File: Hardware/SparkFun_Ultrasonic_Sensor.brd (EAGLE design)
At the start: 44.5 x 21.5 mm, 76 parts, among them J4 Vertical Qwiic Connector, J6 Vertical Qwiic Connector, Q1 600mA/40V, U5 ULTRASONIC_SENSOR_TRANSMITTER, U6 LMV324, U7 STM8L051F3, U8 SP3232EB, U9 ULTRASONIC_SENSOR_RECEIVER

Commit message: Moves the odering instructions away from the design
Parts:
- moved LOGO1 7.62 mm to (57.1, 50.8)
- moved FRAME1 5.24 mm to (77.9, -8.87)
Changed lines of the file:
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@@
 <drawing>
 <settings>
-<setting alwaysvectorfont="no"/>
+<setting alwaysvectorfont="yes"/>
 <setting keepoldvectorfont="yes"/>
 <setting verticaltext="up"/>
@@
 <wire x1="0" y1="21.5392" x2="0" y2="0" width="0.2032" layer="20"/>
 <dimension x1="0" y1="0" x2="0" y2="21.5392" x3="-7.62" y3="10.7696" textsize="1.778" textratio="15" layer="47" unit="inch"/>
-<text x="50.8" y="22.86" size="1.778" layer="51" font="vector">Two Layer
+<text x="58.42" y="22.86" size="1.778" layer="51" font="vector">Two Layer
 1.6mm Thickness
 1 oz. Copper
@@
 HASL Lead Free
 Material: TG135-140</text>
-<text x="102.87" y="-7.62" size="1.778" layer="51" font="vector">NOA Labs</text>
-<text x="84.328" y="-10.16" size="1.778" layer="51" font="vector">Revised By: Elias Santistevan</text>
+<text x="107.95" y="-8.89" size="1.778" layer="51" font="vector">NOA Labs</text>
+<text x="89.408" y="-11.43" size="1.778" layer="51" font="vector">Revised By: Elias Santistevan</text>
 <dimension x1="0" y1="21.5392" x2="44.45" y2="21.5392" x3="22.225" y3="31.75" textsize="1.778" layer="47" unit="inch"/>
 <dimension x1="10.16" y1="12.7" x2="0" y2="12.7" x3="5.08" y3="24.13" textsize="1.778" layer="47" unit="inch"/>
@@
 <attribute name="VALUE" x="38.0746" y="9.8298" size="0.6096" layer="27" font="vector" ratio="20"/>
 </element>
-<element name="FRAME1" library="SparkFun-Aesthetics" package="CREATIVE_COMMONS" value="FRAME-LEDGER" x="72.85" y="-7.6" smashed="yes">
-<attribute name="DESIGNER" value="NOA Labs" x="72.85" y="-7.6" size="1.778" layer="27" display="off"/>
-<attribute name="REV" value="v11" x="72.85" y="-7.6" size="1.778" layer="27" display="off"/>
+<element name="FRAME1" library="SparkFun-Aesthetics" package="CREATIVE_COMMONS" value="FRAME-LEDGER" x="77.93" y="-8.87" smashed="yes">
+<attribute name="DESIGNER" value="NOA Labs" x="77.93" y="-8.87" size="1.778" layer="27" display="off"/>
+<attribute name="REV" value="v11" x="77.93" y="-8.87" size="1.778" layer="27" display="off"/>
 </element>
 <element name="C24" library="SparkFun-Capacitors" package="0603" value="0.1uF" x="34.925" y="12.7" smashed="yes" rot="R270">
@@
 <element name="U$3" library="prod" package="#GND#4" value="" x="19.05" y="3.937" smashed="yes" rot="MR90"/>
 <element name="U$4" library="prod" package="#3V3#2" value="" x="26.67" y="3.937" smashed="yes" rot="MR90"/>
-<element name="LOGO1" library="SparkFun-Aesthetics" package="ORDERING_INSTRUCTIONS" value="SPECIAL_INSTRUCTIONS-ORDERING" x="49.53" y="50.8" smashed="yes"/>
+<element name="LOGO1" library="SparkFun-Aesthetics" package="ORDERING_INSTRUCTIONS" value="SPECIAL_INSTRUCTIONS-ORDERING" x="57.15" y="50.8" smashed="yes"/>
 <element name="LOGO2" library="SparkFun-Aesthetics" package="SFE_LOGO_NAME_.1" value="SFE_LOGO_NAME.1_INCH" x="21.971" y="19.304" smashed="yes" rot="MR0"/>
 <element name="LOGO3" library="SparkFun-Aesthetics" package="QWIIC_3MM" value="QWIIC_LOGO_3MM" x="12.7" y="5.207" smashed="yes"/>

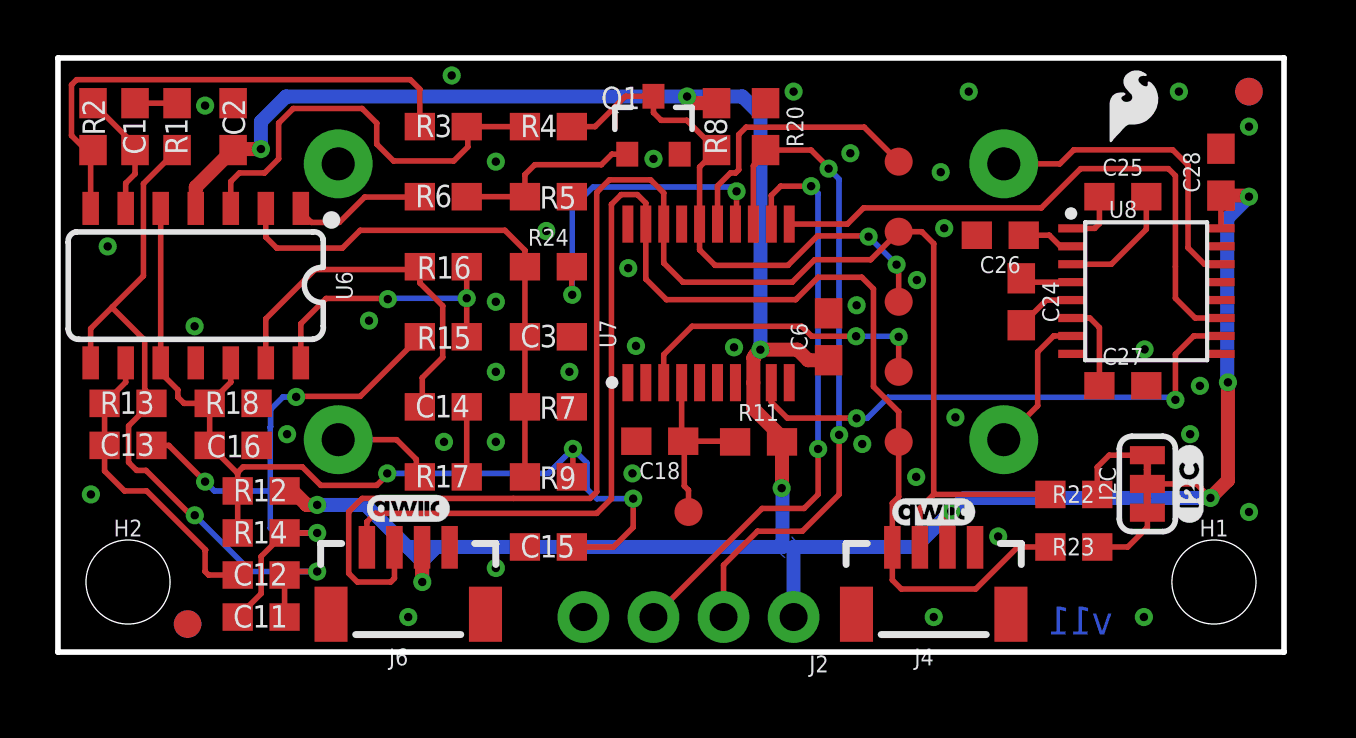
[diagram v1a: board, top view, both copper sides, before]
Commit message: Fixes various schematic elements, some acid traps, and improves ground pour
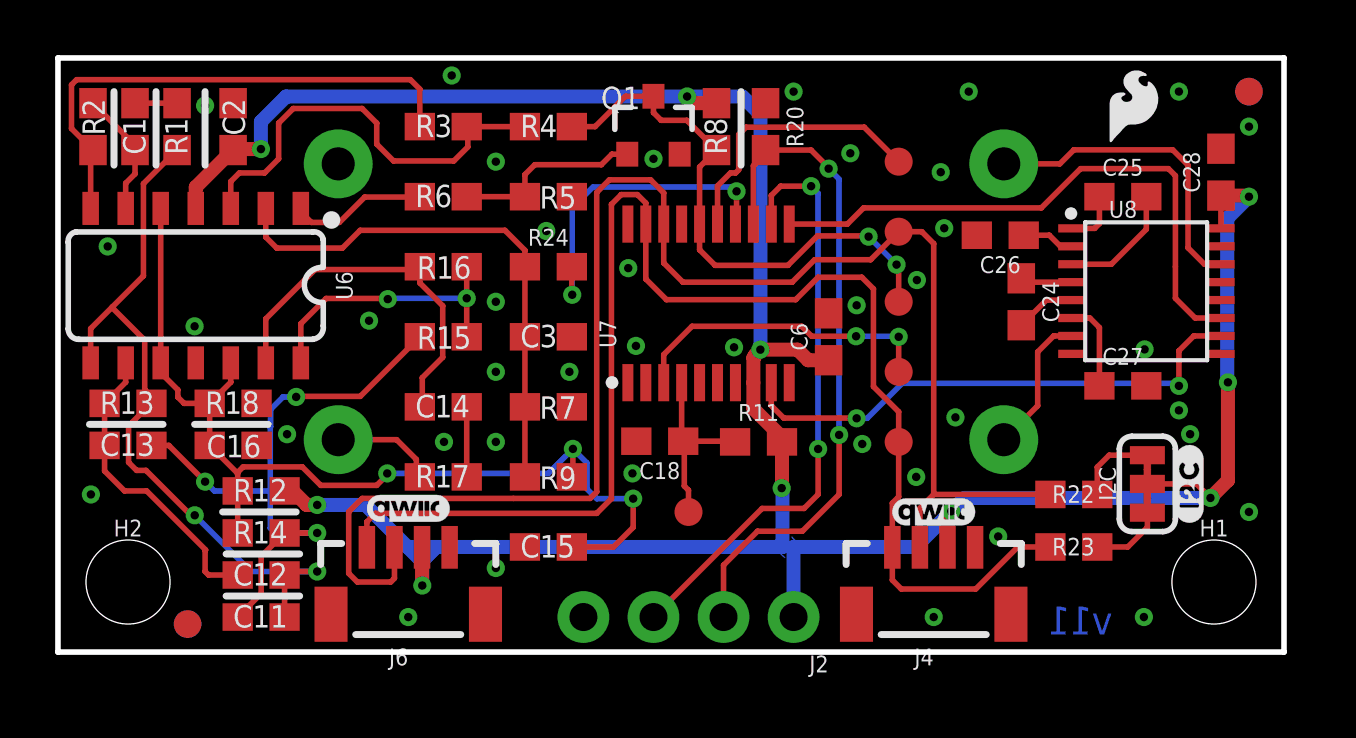
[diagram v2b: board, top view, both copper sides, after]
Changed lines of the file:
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@@
 <drawing>
 <settings>
-<setting alwaysvectorfont="yes"/>
+<setting alwaysvectorfont="no"/>
 <setting keepoldvectorfont="yes"/>
 <setting verticaltext="up"/>
@@
 <layer number="37" name="tTest" color="7" fill="1" visible="no" active="yes"/>
 <layer number="38" name="bTest" color="7" fill="1" visible="no" active="yes"/>
-<layer number="39" name="tKeepout" color="4" fill="11" visible="yes" active="yes"/>
+<layer number="39" name="tKeepout" color="4" fill="11" visible="no" active="yes"/>
 <layer number="40" name="bKeepout" color="1" fill="11" visible="no" active="yes"/>
 <layer number="41" name="tRestrict" color="4" fill="10" visible="no" active="yes"/>
@@
 <layer number="45" name="Holes" color="7" fill="1" visible="yes" active="yes"/>
 <layer number="46" name="Milling" color="3" fill="1" visible="no" active="yes"/>
-<layer number="47" name="Measures" color="7" fill="1" visible="yes" active="yes"/>
+<layer number="47" name="Measures" color="7" fill="1" visible="no" active="yes"/>
 <layer number="48" name="Document" color="7" fill="1" visible="no" active="yes"/>
 <layer number="49" name="Reference" color="13" fill="1" visible="yes" active="yes"/>
 <layer number="50" name="dxf" color="7" fill="1" visible="no" active="no"/>
 <layer number="51" name="tDocu" color="6" fill="1" visible="yes" active="yes"/>
-<layer number="52" name="bDocu" color="7" fill="1" visible="yes" active="yes"/>
+<layer number="52" name="bDocu" color="7" fill="1" visible="no" active="yes"/>
 <layer number="53" name="tGND_GNDA" color="7" fill="9" visible="no" active="no"/>
 <layer number="54" name="bGND_GNDA" color="1" fill="9" visible="no" active="no"/>
@@
 <text x="12.7" y="-19.05" size="1.778" layer="47" font="vector">Units In Inches</text>
 <text x="38.227" y="0.635" size="1.016" layer="16" font="vector" ratio="20" rot="SMR0">v11</text>
+<wire x1="1.143" y1="8.255" x2="3.81" y2="8.255" width="0.254" layer="21"/>
+<wire x1="4.953" y1="8.255" x2="7.62" y2="8.255" width="0.254" layer="21"/>
+<wire x1="5.969" y1="5.08" x2="8.636" y2="5.08" width="0.254" layer="21"/>
+<wire x1="6.096" y1="3.556" x2="8.763" y2="3.556" width="0.254" layer="21"/>
+<wire x1="6.096" y1="2.032" x2="8.763" y2="2.032" width="0.254" layer="21"/>
+<wire x1="2.032" y1="17.653" x2="2.032" y2="20.32" width="0.254" layer="21"/>
+<wire x1="3.556" y1="17.653" x2="3.556" y2="20.32" width="0.254" layer="21"/>
+<wire x1="5.334" y1="17.653" x2="5.334" y2="20.32" width="0.254" layer="21"/>
+<wire x1="24.765" y1="17.653" x2="24.765" y2="20.32" width="0.254" layer="21"/>
 </plain>
 <attributes>
@@
 <via x="29.1592" y="7.5438" extent="1-16" drill="0.3048"/>
 <via x="17.7038" y="15.2654" extent="1-16" drill="0.3048"/>
-<via x="41.402" y="9.652" extent="1-16" drill="0.3048"/>
+<via x="40.64" y="8.763" extent="1-16" drill="0.3048"/>
 <via x="15.875" y="10.16" extent="1-16" drill="0.3048"/>
 <via x="15.875" y="12.7" extent="1-16" drill="0.3048"/>
@@
 <wire x1="12.7762" y1="20.7518" x2="0.67666875" y2="20.7518" width="0.2032" layer="1"/>
 <wire x1="0.67666875" y1="20.7518" x2="0.4906" y2="20.56573125" width="0.2032" layer="1"/>
-<wire x1="0.4906" y1="20.56573125" x2="0.4906" y2="18.72626875" width="0.2032" layer="1"/>
-<wire x1="1.01686875" y1="18.2" x2="1.27" y2="18.2" width="0.2032" layer="1"/>
-<wire x1="0.4906" y1="18.72626875" x2="1.01686875" y2="18.2" width="0.2032" layer="1"/>
+<wire x1="0.4906" y1="20.56573125" x2="0.4906" y2="18.98026875" width="0.2032" layer="1"/>
+<wire x1="1.27" y1="18.2" x2="1.27" y2="18.20086875" width="0.2032" layer="1"/>
+<wire x1="1.27" y1="18.20086875" x2="0.4906" y2="18.98026875" width="0.2032" layer="1"/>
 </signal>
 <signal name="N$2">
@@
 <contactref element="U8" pad="P10"/>
 <wire x1="42.163" y1="11.461" x2="41.179" y2="11.461" width="0.2032" layer="1"/>
-<wire x1="40.513" y1="10.795" x2="40.513" y2="9.144" width="0.2032" layer="1"/>
-<wire x1="41.179" y1="11.461" x2="40.513" y2="10.795" width="0.2032" layer="1"/>
-<wire x1="25.862" y1="9.767" x2="25.862" y2="9.063" width="0.2032" layer="1"/>
+<wire x1="40.64" y1="10.922" x2="40.64" y2="9.652" width="0.2032" layer="1"/>
+<wire x1="41.179" y1="11.461" x2="40.64" y2="10.922" width="0.2032" layer="1"/>
+<wire x1="25.862" y1="9.767" x2="25.862" y2="8.936" width="0.2032" layer="1"/>
 <via x="28.956" y="8.4752" extent="1-16" drill="0.3048"/>
 <wire x1="28.9476" y1="8.4836" x2="28.956" y2="8.4752" width="0.2032" layer="1"/>
-<wire x1="28.9476" y1="8.4836" x2="26.4414" y2="8.4836" width="0.2032" layer="1"/>
-<via x="40.513" y="9.144" extent="1-16" drill="0.3048"/>
-<wire x1="25.862" y1="9.063" x2="26.4414" y2="8.4836" width="0.2032" layer="1"/>
-<wire x1="40.4198" y1="9.2372" x2="30.099" y2="9.2372" width="0.2032" layer="16"/>
-<wire x1="30.099" y1="9.2372" x2="29.337" y2="8.4752" width="0.2032" layer="16"/>
+<wire x1="28.9476" y1="8.4836" x2="26.3144" y2="8.4836" width="0.2032" layer="1"/>
+<via x="40.64" y="9.652" extent="1-16" drill="0.3048"/>
+<wire x1="25.862" y1="8.936" x2="26.3144" y2="8.4836" width="0.2032" layer="1"/>
+<wire x1="40.5468" y1="9.7452" x2="30.607" y2="9.7452" width="0.2032" layer="16"/>
+<wire x1="30.607" y1="9.7452" x2="29.337" y2="8.4752" width="0.2032" layer="16"/>
 <wire x1="28.956" y1="8.4752" x2="29.337" y2="8.4752" width="0.2032" layer="16"/>
-<wire x1="40.4198" y1="9.2372" x2="40.513" y2="9.144" width="0.2032" layer="16"/>
+<wire x1="40.5468" y1="9.7452" x2="40.64" y2="9.652" width="0.2032" layer="16"/>
 </signal>
 <signal name="DIN1">
@@
 <wire x1="9.017" y1="5.334" x2="8.509" y2="5.842" width="0.508" layer="1"/>
 <wire x1="8.509" y1="5.842" x2="8.216" y2="5.842" width="0.508" layer="1"/>
-<wire x1="13.2" y1="3.797" x2="13.2" y2="2.548" width="0.508" layer="1"/>
-<wire x1="13.2" y1="2.548" x2="13.208" y2="2.54" width="0.508" layer="1"/>
-<via x="13.208" y="2.54" extent="1-16" drill="0.3048"/>
-<wire x1="13.208" y1="2.54" x2="13.208" y2="3.302" width="0.508" layer="16"/>
+<wire x1="13.2" y1="3.797" x2="13.2" y2="2.421" width="0.508" layer="1"/>
+<wire x1="13.2" y1="2.421" x2="13.208" y2="2.413" width="0.508" layer="1"/>
+<via x="13.208" y="2.413" extent="1-16" drill="0.3048"/>
+<wire x1="13.208" y1="2.413" x2="13.208" y2="3.302" width="0.508" layer="16"/>
 </signal>
 <signal name="ADDR_RST">

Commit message: Moves a number of parts to away from the Ultrasonic sensor plated holes
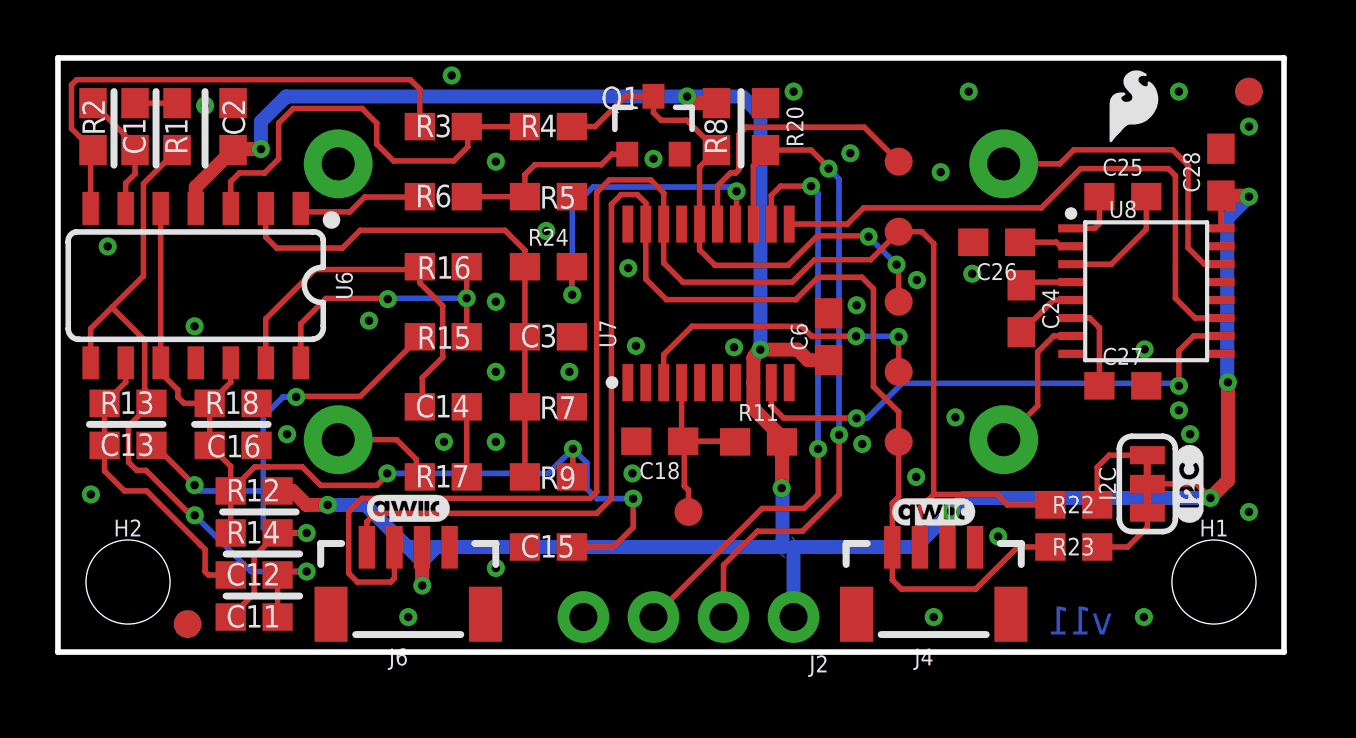
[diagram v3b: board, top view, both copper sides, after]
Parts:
- moved R22 0.38 mm to (36.8, 5.33)
- moved C26 0.28 mm to (34.0, 14.9)
- moved C11 0.25 mm to (7.11, 1.27)
- moved C12 0.25 mm to (7.11, 2.79)
- moved C24 0.25 mm to (34.9, 12.4)
- moved R12 0.25 mm to (7.11, 5.84)
- moved R14 0.25 mm to (7.11, 4.32)
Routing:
- net N$10: track 26.8 -> 26.3 mm

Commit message: Moves some more parts away from the sensor through holes and updates the schematic
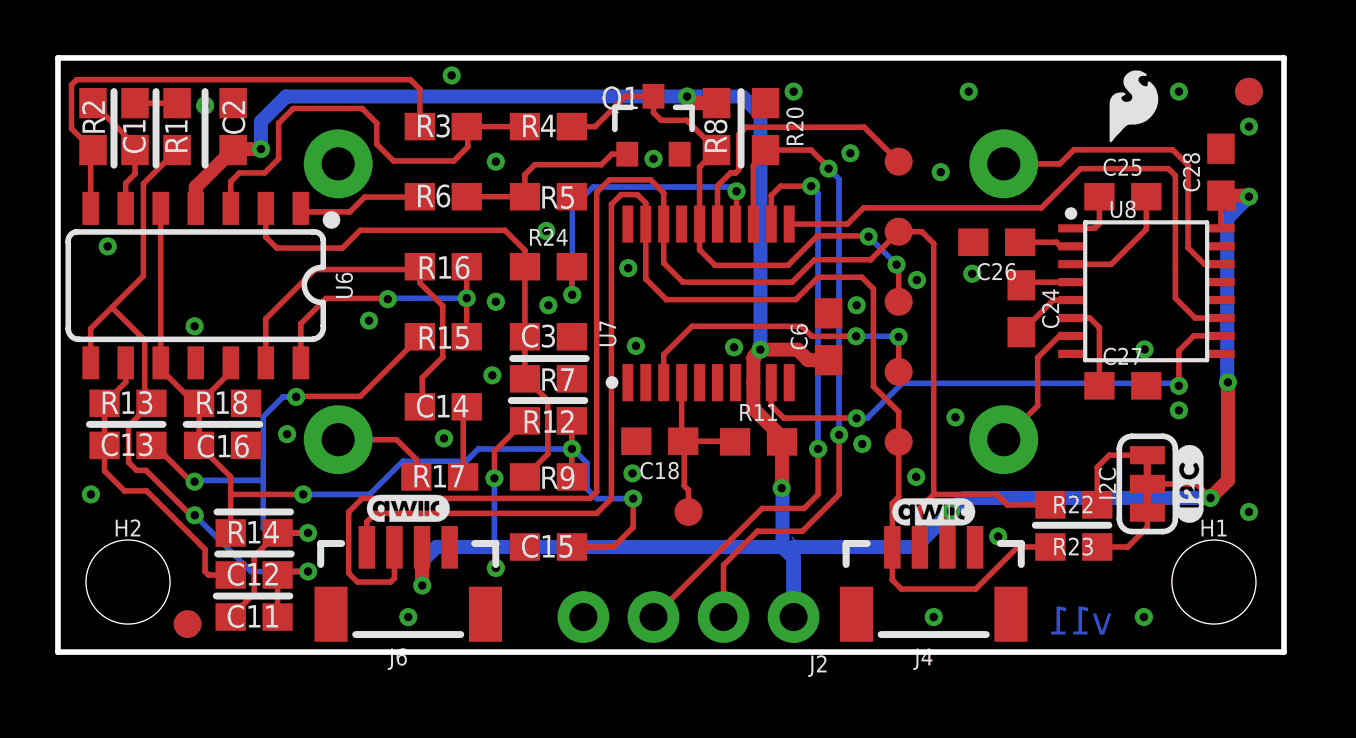
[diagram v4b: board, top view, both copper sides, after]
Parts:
- added U$13: (no value), prod:DEFAULT129
- added U$14: (no value), prod:ADDR#130
- added U$15: (no value), prod:0X2F131
- moved R12 11.0 mm to (17.8, 8.38), turned to 180 degrees
- moved R7 1.02 mm to (17.8, 9.91)
- moved C16 0.38 mm to (5.97, 7.49)
- moved R18 0.38 mm to (5.97, 9.02)
- moved R17 0.13 mm to (13.8, 6.35)
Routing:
- net PB4: track 19.4 -> 20.1 mm

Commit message: Adds power LED, RXT silk, and increases the size of the tespoints.
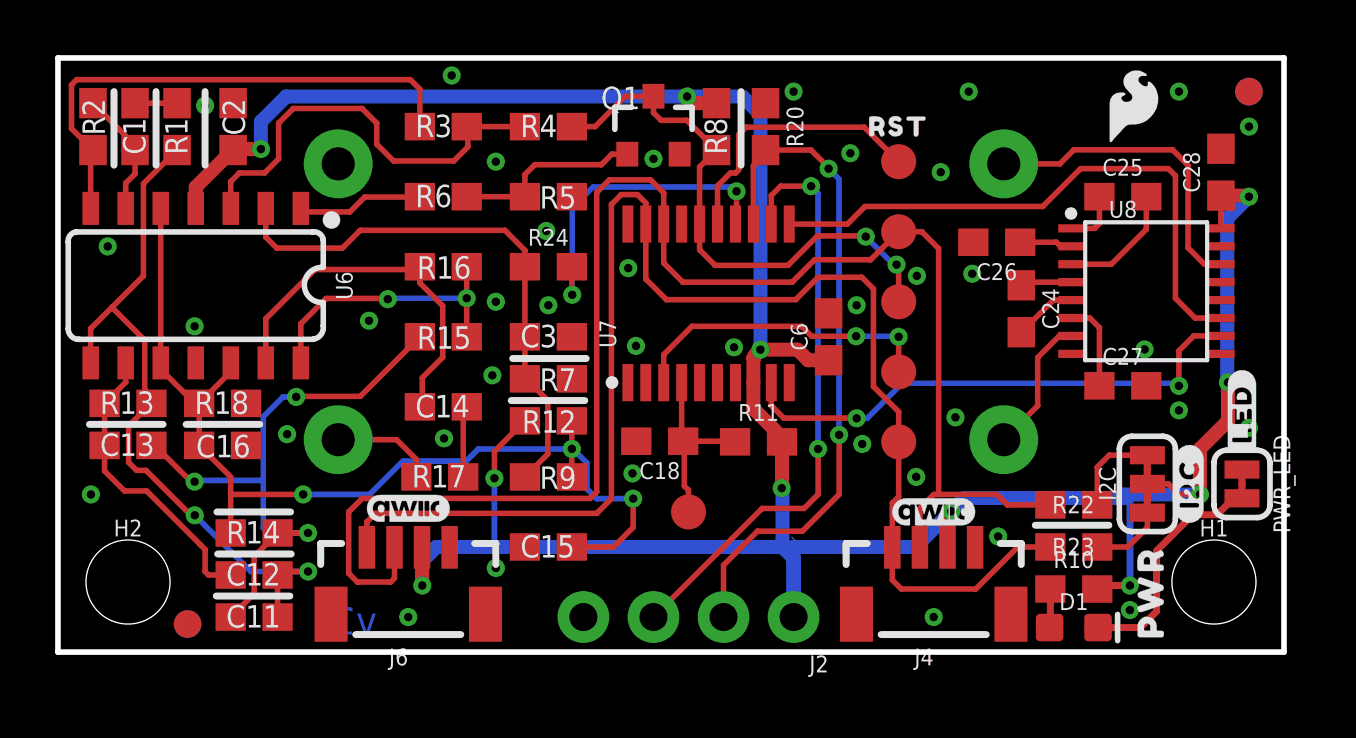
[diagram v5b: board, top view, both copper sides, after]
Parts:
- added D1: Red, SparkFun-LED:LED-0603
- added PWR_LED: JUMPER-SMT_2_NC_TRACE_SILK, SparkFun-Jumpers:SMT-JUMPER_2_NC_TRACE_SILK
- added R10: 4.7k, SparkFun-Resistors:0603
- added U$16: (no value), top:PWR17
- added U$17: (no value), top:#LED#15
- added U$18: (no value), prod:RST132
- TP1, TP2, TP3, TP4, TP5, TP6: value TEST-POINT3X4 -> TEST-POINT3X5; device SparkFun-Connectors:PAD.03X.04 -> SparkFun-Connectors:PAD.03X.05
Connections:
- new net N$11: D1.C, PWR_LED.2
- new net N$7: D1.A, R10.1
- net 3.3V: now also R10.2
- net GND: now also PWR_LED.1
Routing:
- net N$11: track 0.00 -> 8.45 mm
- net 3.3V: track 102.8 -> 106.8 mm, vias 10 -> 11
- net N$7: track 0.00 -> 1.41 mm
